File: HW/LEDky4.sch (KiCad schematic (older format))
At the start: 8 parts

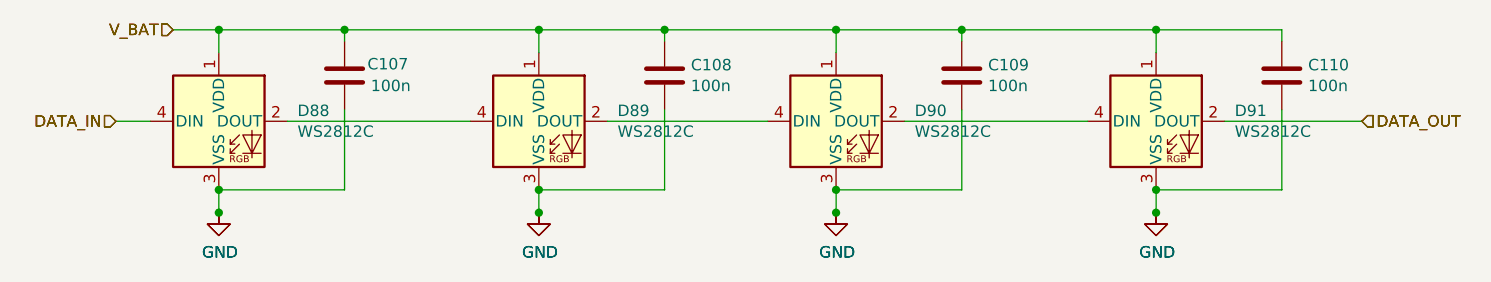
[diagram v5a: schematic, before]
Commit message: make schematic beautiful (for printing)
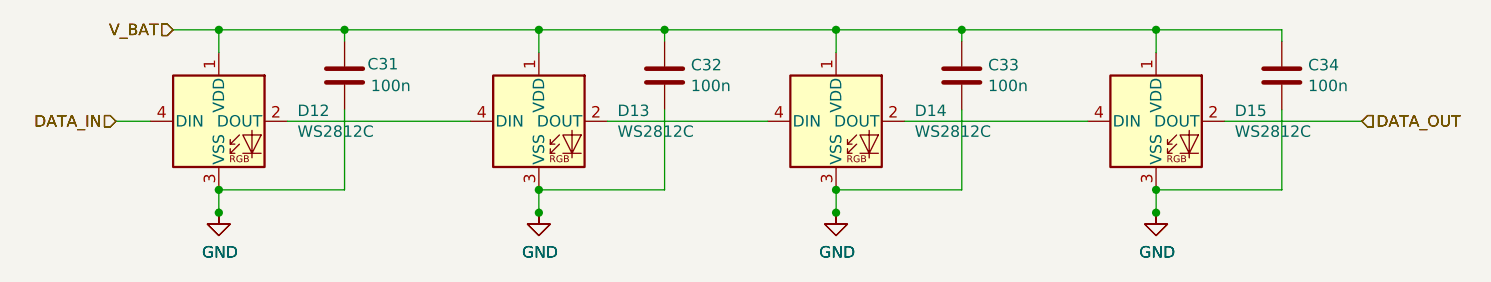
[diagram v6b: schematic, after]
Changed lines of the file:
@@
 $Descr A4 11693 8268
 encoding utf-8
-Sheet 7 28
+Sheet 6 28
 Title ""
 Date ""
@@
 AR Path="/5F79BCD0/5FB77CB0/5F78FD5C" Ref="#PWR0122"  Part="1"
 AR Path="/5FACC290/5FB77CB0/5F78FD5C" Ref="#PWR0207"  Part="1"
-F 0 "#PWR0207" H 3700 3850 50  0001 C CNN
+F 0 "#PWR050" H 3700 3850 50  0001 C CNN
 F 1 "GND" H 3705 3927 50  0000 C CNN
 F 2 "" H 3700 4100 50  0001 C CNN
@@
 AR Path="/5F79BCD0/5FB77CB0/5F78FD62" Ref="C67"  Part="1"
 AR Path="/5FACC290/5FB77CB0/5F78FD62" Ref="C107"  Part="1"
-F 0 "C107" H 4350 3550 50  0000 L CNN
+F 0 "C31" H 4350 3550 50  0000 L CNN
 F 1 "100n" H 4365 3455 50  0000 L CNN
 F 2 "Capacitor_SMD:C_0402_1005Metric" H 4288 3350 50  0001 C CNN
@@
 AR Path="/5F79BCD0/5FB77CB0/5F78FD71" Ref="D49"  Part="1"
 AR Path="/5FACC290/5FB77CB0/5F78FD71" Ref="D89"  Part="1"
-F 0 "D89" H 5444 3746 50  0000 L CNN
+F 0 "D13" H 5444 3746 50  0000 L CNN
 F 1 "WS2812C" H 5444 3655 50  0000 L CNN
 F 2 "LED_SMD:LED_WS2812B_PLCC4_5.0x5.0mm_P3.2mm" H 5150 3400 50  0001 L TNN
@@
 AR Path="/5F79BCD0/5FB77CB0/5F798BEB" Ref="#PWR0125"  Part="1"
 AR Path="/5FACC290/5FB77CB0/5F798BEB" Ref="#PWR0210"  Part="1"
-F 0 "#PWR0210" H 5100 3850 50  0001 C CNN
+F 0 "#PWR053" H 5100 3850 50  0001 C CNN
 F 1 "GND" H 5105 3927 50  0000 C CNN
 F 2 "" H 5100 4100 50  0001 C CNN
@@
 AR Path="/5F79BCD0/5FB77CB0/5F798BEE" Ref="#PWR0127"  Part="1"
 AR Path="/5FACC290/5FB77CB0/5F798BEE" Ref="#PWR0212"  Part="1"
-F 0 "#PWR0212" H 6400 3850 50  0001 C CNN
+F 0 "#PWR055" H 6400 3850 50  0001 C CNN
 F 1 "GND" H 6405 3927 50  0000 C CNN
 F 2 "" H 6400 4100 50  0001 C CNN
@@
 AR Path="/5F79BCD0/5FB77CB0/5F78FDA5" Ref="D51"  Part="1"
 AR Path="/5FACC290/5FB77CB0/5F78FDA5" Ref="D91"  Part="1"
-F 0 "D91" H 8144 3746 50  0000 L CNN
+F 0 "D15" H 8144 3746 50  0000 L CNN
 F 1 "WS2812C" H 8144 3655 50  0000 L CNN
 F 2 "LED_SMD:LED_WS2812B_PLCC4_5.0x5.0mm_P3.2mm" H 7850 3400 50  0001 L TNN
@@
 AR Path="/5F79BCD0/5FB77CB0/5F78FDAB" Ref="#PWR0128"  Part="1"
 AR Path="/5FACC290/5FB77CB0/5F78FDAB" Ref="#PWR0213"  Part="1"
-F 0 "#PWR0213" H 7800 3850 50  0001 C CNN
+F 0 "#PWR056" H 7800 3850 50  0001 C CNN
 F 1 "GND" H 7805 3927 50  0000 C CNN
 F 2 "" H 7800 4100 50  0001 C CNN
@@
 AR Path="/5F79BCD0/5FB77CB0/5F78FDB1" Ref="C70"  Part="1"
 AR Path="/5FACC290/5FB77CB0/5F78FDB1" Ref="C110"  Part="1"
-F 0 "C110" H 8465 3546 50  0000 L CNN
+F 0 "C34" H 8465 3546 50  0000 L CNN
 F 1 "100n" H 8465 3455 50  0000 L CNN
 F 2 "Capacitor_SMD:C_0402_1005Metric" H 8388 3350 50  0001 C CNN
@@
 AR Path="/5F79BCD0/5FB77CB0/5F78FD56" Ref="D48"  Part="1"
 AR Path="/5FACC290/5FB77CB0/5F78FD56" Ref="D88"  Part="1"
-F 0 "D88" H 4044 3746 50  0000 L CNN
+F 0 "D12" H 4044 3746 50  0000 L CNN
 F 1 "WS2812C" H 4044 3655 50  0000 L CNN
 F 2 "LED_SMD:LED_WS2812B_PLCC4_5.0x5.0mm_P3.2mm" H 3750 3400 50  0001 L TNN
@@
 AR Path="/5F79BCD0/5FB77CB0/5F798BE8" Ref="#PWR0123"  Part="1"
 AR Path="/5FACC290/5FB77CB0/5F798BE8" Ref="#PWR0208"  Part="1"
-F 0 "#PWR0208" H 3700 3850 50  0001 C CNN
+F 0 "#PWR051" H 3700 3850 50  0001 C CNN
 F 1 "GND" H 3705 3927 50  0000 C CNN
 F 2 "" H 3700 4100 50  0001 C CNN
@@
 AR Path="/5F79BCD0/5FB77CB0/5F78FD77" Ref="#PWR0124"  Part="1"
 AR Path="/5FACC290/5FB77CB0/5F78FD77" Ref="#PWR0209"  Part="1"
-F 0 "#PWR0209" H 5100 3850 50  0001 C CNN
+F 0 "#PWR052" H 5100 3850 50  0001 C CNN
 F 1 "GND" H 5105 3927 50  0000 C CNN
 F 2 "" H 5100 4100 50  0001 C CNN
@@
 AR Path="/5F79BCD0/5FB77CB0/5F78FD7D" Ref="C68"  Part="1"
 AR Path="/5FACC290/5FB77CB0/5F78FD7D" Ref="C108"  Part="1"
-F 0 "C108" H 5765 3546 50  0000 L CNN
+F 0 "C32" H 5765 3546 50  0000 L CNN
 F 1 "100n" H 5765 3455 50  0000 L CNN
 F 2 "Capacitor_SMD:C_0402_1005Metric" H 5688 3350 50  0001 C CNN
@@
 AR Path="/5F79BCD0/5FB77CB0/5F78FD8B" Ref="D50"  Part="1"
 AR Path="/5FACC290/5FB77CB0/5F78FD8B" Ref="D90"  Part="1"
-F 0 "D90" H 6744 3746 50  0000 L CNN
+F 0 "D14" H 6744 3746 50  0000 L CNN
 F 1 "WS2812C" H 6744 3655 50  0000 L CNN
 F 2 "LED_SMD:LED_WS2812B_PLCC4_5.0x5.0mm_P3.2mm" H 6450 3400 50  0001 L TNN
@@
 AR Path="/5F79BCD0/5FB77CB0/5F78FD91" Ref="#PWR0126"  Part="1"
 AR Path="/5FACC290/5FB77CB0/5F78FD91" Ref="#PWR0211"  Part="1"
-F 0 "#PWR0211" H 6400 3850 50  0001 C CNN
+F 0 "#PWR054" H 6400 3850 50  0001 C CNN
 F 1 "GND" H 6405 3927 50  0000 C CNN
 F 2 "" H 6400 4100 50  0001 C CNN
@@
 AR Path="/5F79BCD0/5FB77CB0/5F78FD97" Ref="C69"  Part="1"
 AR Path="/5FACC290/5FB77CB0/5F78FD97" Ref="C109"  Part="1"
-F 0 "C109" H 7065 3546 50  0000 L CNN
+F 0 "C33" H 7065 3546 50  0000 L CNN
 F 1 "100n" H 7065 3455 50  0000 L CNN
 F 2 "Capacitor_SMD:C_0402_1005Metric" H 6988 3350 50  0001 C CNN
@@
 AR Path="/5F79BCD0/5FB77CB0/5F798BF1" Ref="#PWR0129"  Part="1"
 AR Path="/5FACC290/5FB77CB0/5F798BF1" Ref="#PWR0214"  Part="1"
-F 0 "#PWR0214" H 7800 3850 50  0001 C CNN
+F 0 "#PWR057" H 7800 3850 50  0001 C CNN
 F 1 "GND" H 7805 3927 50  0000 C CNN
 F 2 "" H 7800 4100 50  0001 C CNN
